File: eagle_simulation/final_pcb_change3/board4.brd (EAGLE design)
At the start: 59.4 x 54.6 mm, 11 parts, among them U3 R-78E5.0-1.0

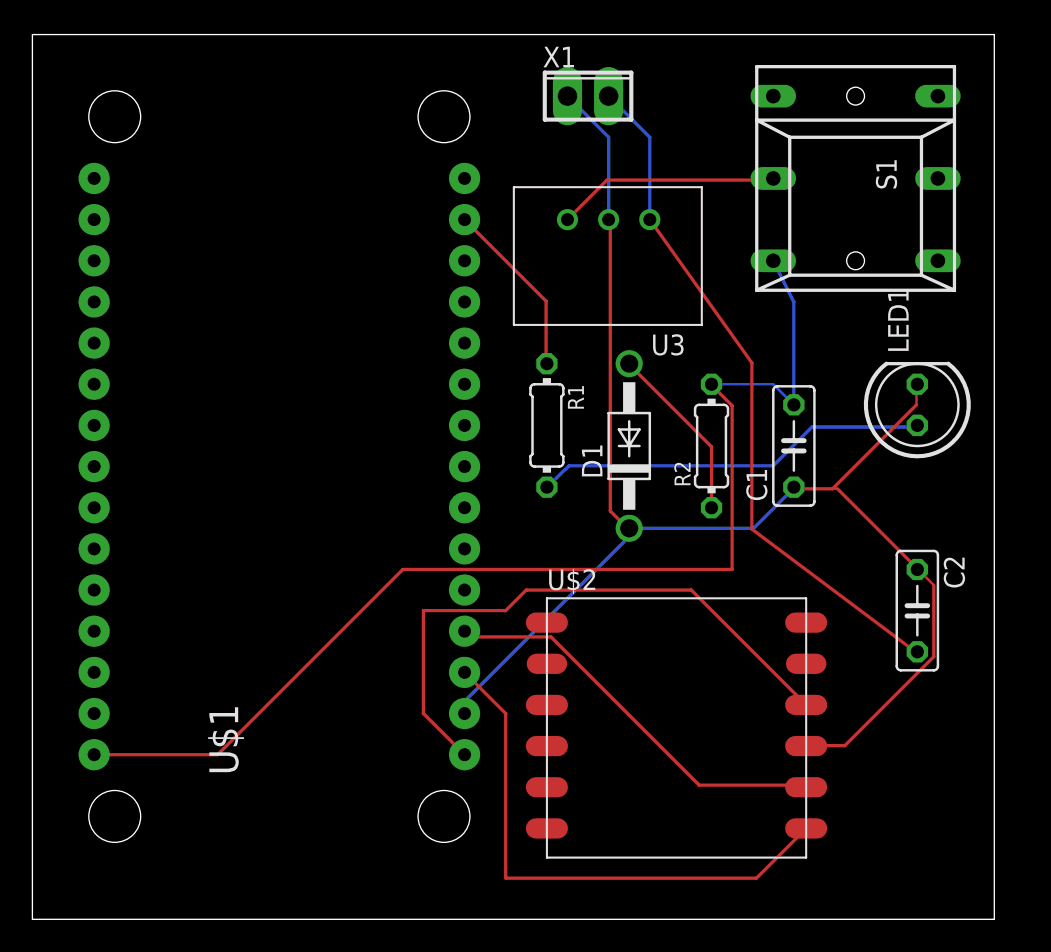
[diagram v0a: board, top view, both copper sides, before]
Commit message: edited forgot-password.php and added some files
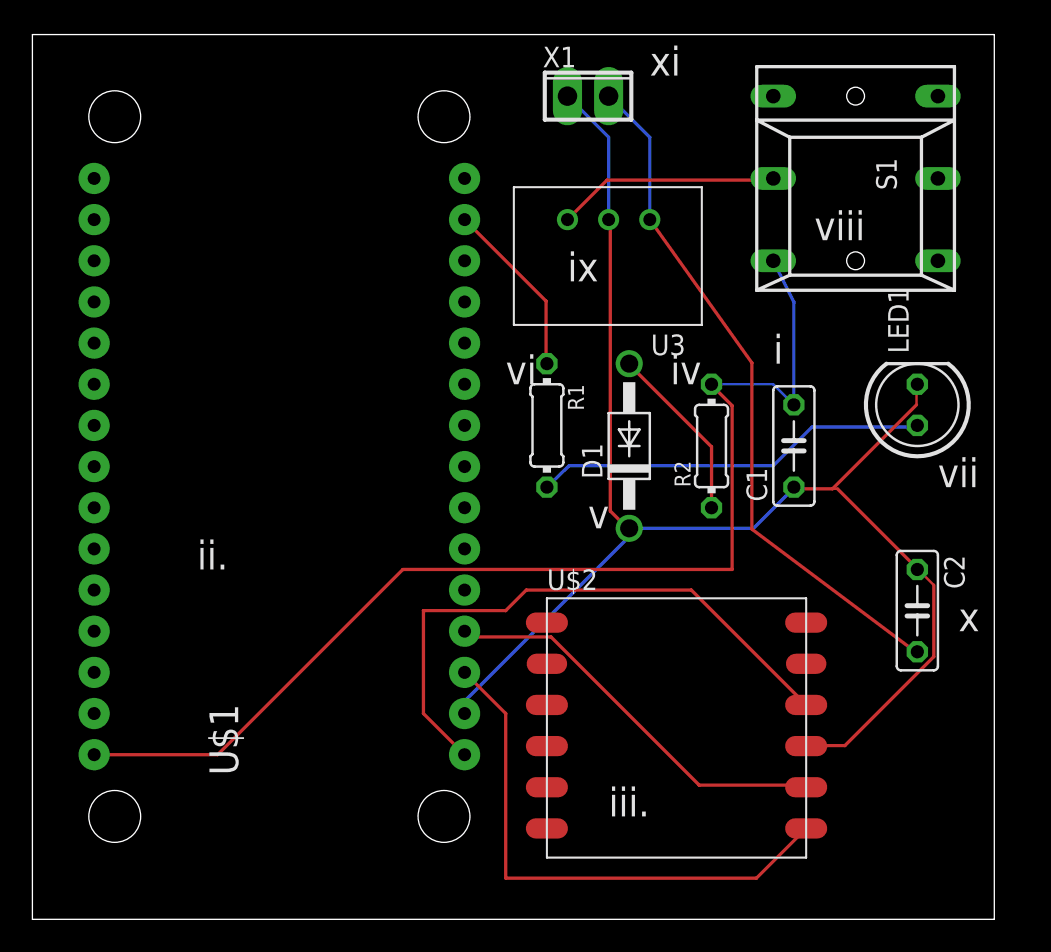
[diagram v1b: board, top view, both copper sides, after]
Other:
- board text added: "i"
- board text added: "ii."
- board text added: "iii."
- board text added: "iv"
- board text added: "ix"
- board text added: "v"
- board text added: "vi"
- board text added: "vii"
- board text added: "viii"
- board text added: "x"
- board text added: "xi"
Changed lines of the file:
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@@
 <?xml version="1.0" encoding="utf-8"?>
 <!DOCTYPE eagle SYSTEM "eagle.dtd">
-<eagle version="8.5.0">
+<eagle version="9.0.1">
 <drawing>
 <settings>
@@
 <wire x1="59.36" y1="80" x2="0" y2="80" width="0" layer="20"/>
 <wire x1="0" y1="80" x2="0" y2="25.4" width="0" layer="20"/>
+<text x="10.16" y="46.99" size="1.778" layer="25">ii.</text>
+<text x="35.56" y="31.75" size="1.778" layer="25">iii.</text>
+<text x="39.37" y="58.42" size="1.778" layer="25">iv</text>
+<text x="34.29" y="49.53" size="1.778" layer="25">v</text>
+<text x="29.21" y="58.42" size="1.778" layer="25">vi</text>
+<text x="55.88" y="52.07" size="1.778" layer="25">vii</text>
+<text x="48.26" y="67.31" size="1.778" layer="25">viii</text>
+<text x="33.02" y="64.77" size="1.778" layer="25">ix</text>
+<text x="57.15" y="43.18" size="1.778" layer="25">x</text>
+<text x="38.1" y="77.47" size="1.778" layer="25">xi</text>
+<text x="45.72" y="59.69" size="1.778" layer="25">i</text>
 </plain>
 <attributes>
